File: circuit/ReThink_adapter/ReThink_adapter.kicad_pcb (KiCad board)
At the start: 2 copper layers, 69 parts, among them J1 FH34SRJ-34S-0.5SH(50), J2 FH34SRJ-6S-0.5SH(50), J3 Mezzanine, J4 XF3M(1)-3015-1B, J5 XF3M(1)-0815-1B, J6 FH34SRJ-40S-0.5SH(50), J7 FH52-40S-0.5SH, J8 XF3M(1)-1415-1B, U1 PCAL6416AHF, U2 LM2775DSG, U3 PCA9306, U4 TPS610333DRLR

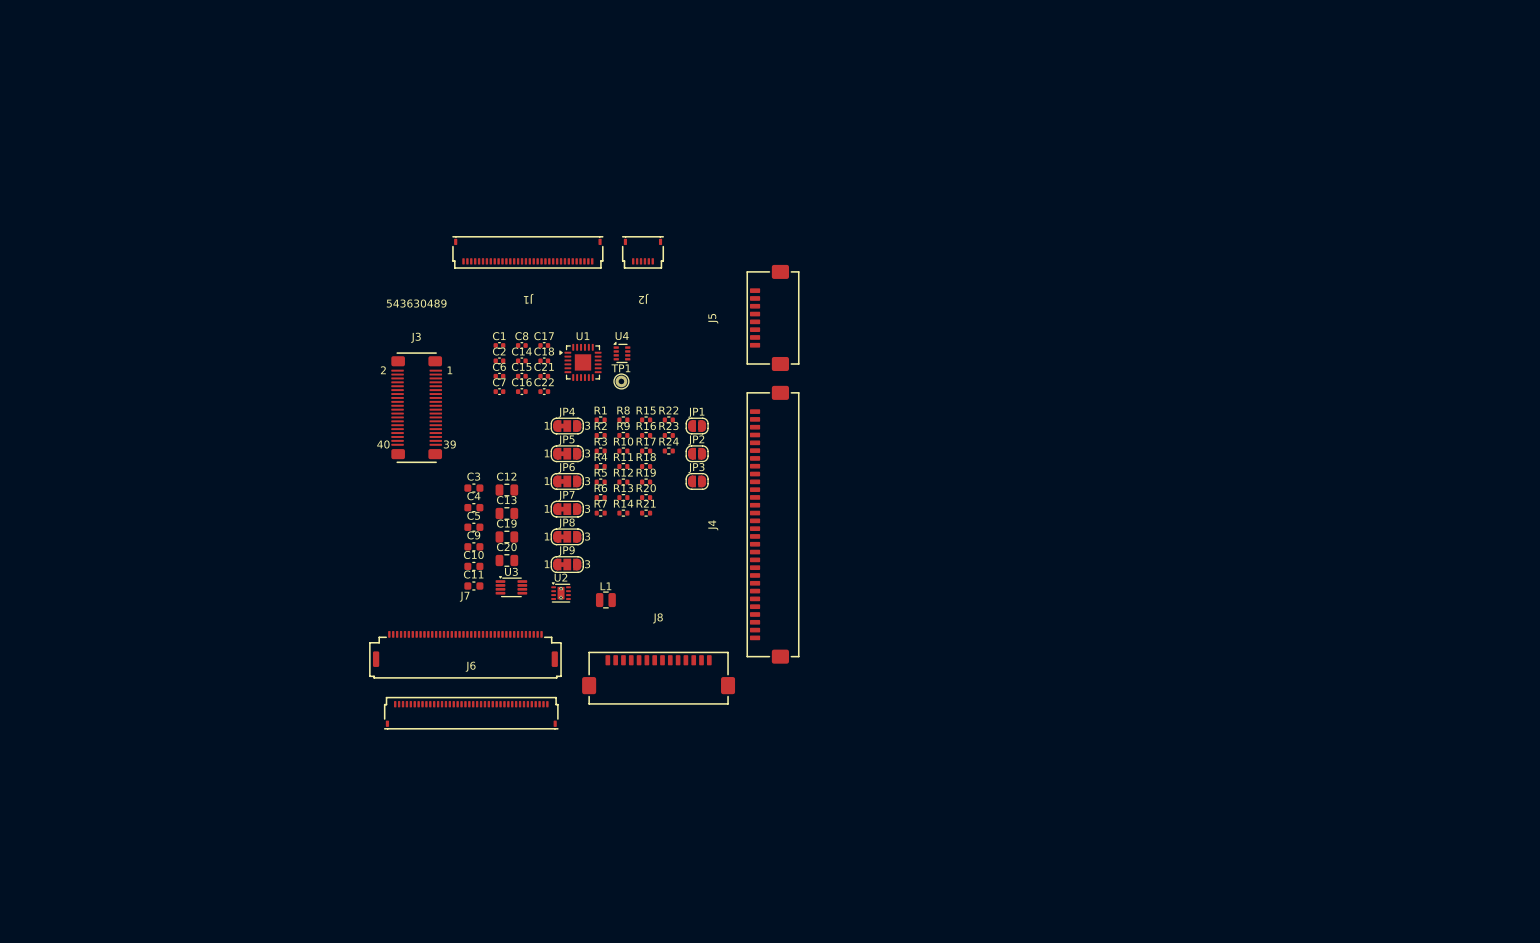
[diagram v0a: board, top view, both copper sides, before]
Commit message: group connectors on PCB
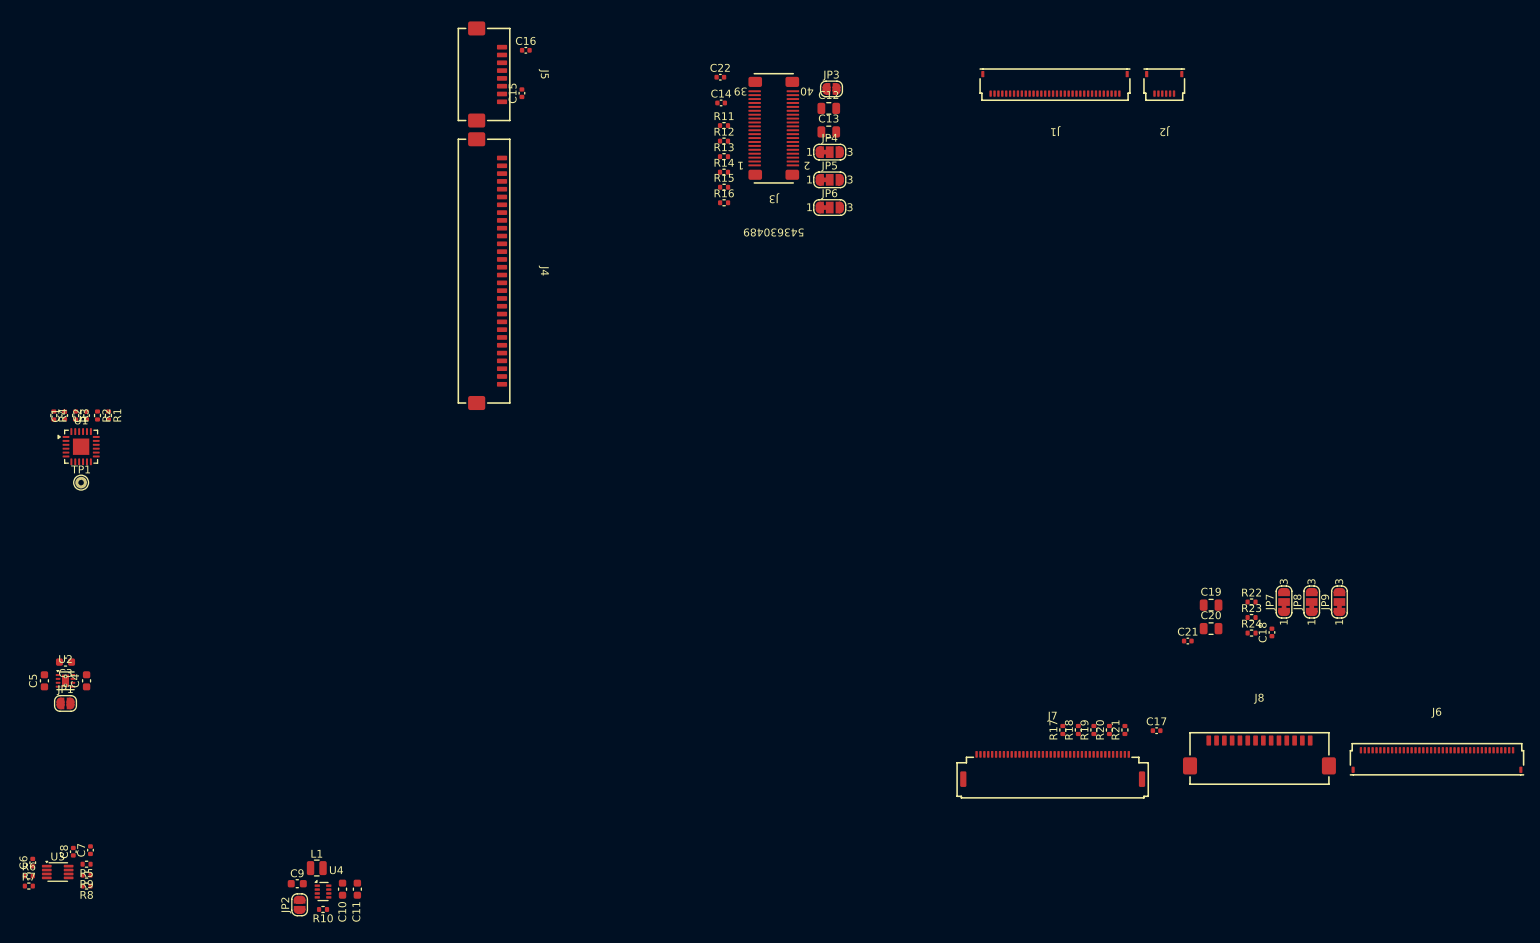
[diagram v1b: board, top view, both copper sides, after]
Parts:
- moved J6 123.9 mm to (212.8, 151.5)
- moved C18 99.5 mm to (191.6, 136.8), turned to 90 degrees
- moved JP9 99.1 mm to (200.2, 132.9), turned to 90 degrees
- moved JP8 95.8 mm to (196.7, 132.9), turned to 90 degrees
- moved C17 92.7 mm to (176.8, 149.4)
- moved JP7 92.6 mm to (193.2, 132.9), turned to 90 degrees
- moved R8 91.1 mm to (39.7, 169.3), turned to 180 degrees
- moved C19 90.7 mm to (183.8, 133.3)
- moved C20 90.7 mm to (183.8, 136.3)
- moved C21 89.2 mm to (180.8, 137.9)
- moved R9 88.9 mm to (39.7, 167.9), turned to 180 degrees
- moved JP1 88.4 mm to (37.0, 145.9)
- moved R6 87.9 mm to (32.3, 168.0)
- moved R7 87.5 mm to (32.3, 169.3)
- moved C8 86.7 mm to (38.0, 164.9), turned to 90 degrees
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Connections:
- J2 pad 1: GND -> VIN
- J2 pad 2: GND -> VIN
- J2 pad 5: VIN -> GND
- J2 pad 6: VIN -> GND
- J5 pad 1: TP1_PWR -> /TP1_DAT
- J5 pad 2: GND -> /TP1_RST
- J5 pad 3: /TP1_CLK -> /MIDDLE
- J5 pad 4: /LEFT -> /RIGHT
- J5 pad 5: /RIGHT -> /LEFT
- J5 pad 6: /MIDDLE -> /TP1_CLK
- J5 pad 7: /TP1_RST -> GND
- J5 pad 8: /TP1_DAT -> TP1_PWR
- J6 pad 10: /SENSE2 -> /HOTKEY
- J6 pad 11: /SENSE0 -> Net-(J6-Pin_11)
- J6 pad 12: /DRV4 -> Net-(J6-Pin_12)
- J6 pad 13: /DRV2 -> Net-(J6-Pin_13)
- J6 pad 14: /SENSE5 -> LED_3V3
- J6 pad 15: /DRV1 -> /DRV11
- J6 pad 16: /DRV3 -> /DRV8
- J6 pad 17: /DRV6 -> /DRV10
- J6 pad 18: /DRV7 -> /DRV12
- J6 pad 19: /DRV5 -> /DRV9
- J6 pad 20: /DRV15 -> /DRV13
- J6 pad 21: /DRV13 -> /DRV15
- J6 pad 22: /DRV9 -> /DRV5
- J6 pad 23: /DRV12 -> /DRV7
- J6 pad 24: /DRV10 -> /DRV6
- J6 pad 25: /DRV8 -> /DRV3
- J6 pad 26: /DRV11 -> /DRV1
- J6 pad 27: LED_3V3 -> /SENSE5
- J6 pad 28: Net-(J6-Pin_28) -> /DRV2
- J6 pad 29: Net-(J6-Pin_29) -> /DRV4
- J6 pad 3: /SENSE3 -> /DRV16
- J6 pad 30: Net-(J6-Pin_30) -> /SENSE0
- J6 pad 31: /HOTKEY -> /SENSE2
- J6 pad 32: GND -> /DRV0
- J6 pad 33: Net-(J6-Pin_33) -> /SENSE1
- J6 pad 34: GND -> /SENSE4
- J6 pad 35: /LEFT -> /DRV14
- J6 pad 36: /RIGHT -> /SENSE6
- J6 pad 37: /MIDDLE -> /SENSE7
- J6 pad 38: /DRV16 -> /SENSE3
- J6 pad 4: /SENSE7 -> /MIDDLE
- J6 pad 5: /SENSE6 -> /RIGHT
- J6 pad 6: /DRV14 -> /LEFT
- J6 pad 7: /SENSE4 -> GND
- J6 pad 8: /SENSE1 -> Net-(J6-Pin_8)
- J6 pad 9: /DRV0 -> GND
- J7 pad 26: Net-(J6-Pin_28) -> Net-(J6-Pin_13)
- J7 pad 27: Net-(J6-Pin_29) -> Net-(J6-Pin_12)
- J7 pad 28: Net-(J6-Pin_30) -> Net-(J6-Pin_11)
- J7 pad 31: Net-(J6-Pin_33) -> Net-(J6-Pin_8)
- J8 pad 1: TP2_PWR -> unconnected-(J8-Pin_1-Pad1)
- J8 pad 10: /PWM -> BL_5V
- J8 pad 11: /KBD_BL_DTCT -> /PWM
- J8 pad 12: GND -> /KBD_BL_DTCT
- J8 pad 13: (no net) -> GND
- J8 pad 14: (no net) -> unconnected-(J8-Pin_14-Pad14)
- J8 pad 2: /TP2_DAT -> TP2_PWR
- J8 pad 3: /TP2_RST -> /TP2_DAT
- J8 pad 4: /MIDDLE -> /TP2_RST
- J8 pad 5: /RIGHT -> /MIDDLE
- J8 pad 6: /LEFT -> /RIGHT
- J8 pad 7: GND -> /LEFT
- J8 pad 8: /TP2_CLK -> GND
- J8 pad 9: BL_5V -> /TP2_CLK
- R17 pad 1: Net-(J6-Pin_28) -> Net-(J6-Pin_13)
- R18 pad 1: Net-(J6-Pin_29) -> Net-(J6-Pin_12)
- R19 pad 1: Net-(J6-Pin_30) -> Net-(J6-Pin_11)
- R20 pad 1: Net-(J6-Pin_33) -> Net-(J6-Pin_8)
- R24 pad 2: GND -> unconnected-(R24-Pad2)
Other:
- board text added: "Connector orientation: Good Placement: Grouped"
- board text added: "Connector orientation: Good Placement: Not checked"
- board text added: "Connector orientation: Not checked Placement: Grouped"
- board text added: "Max height: 1.5mm"

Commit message: added JLCPCB rules
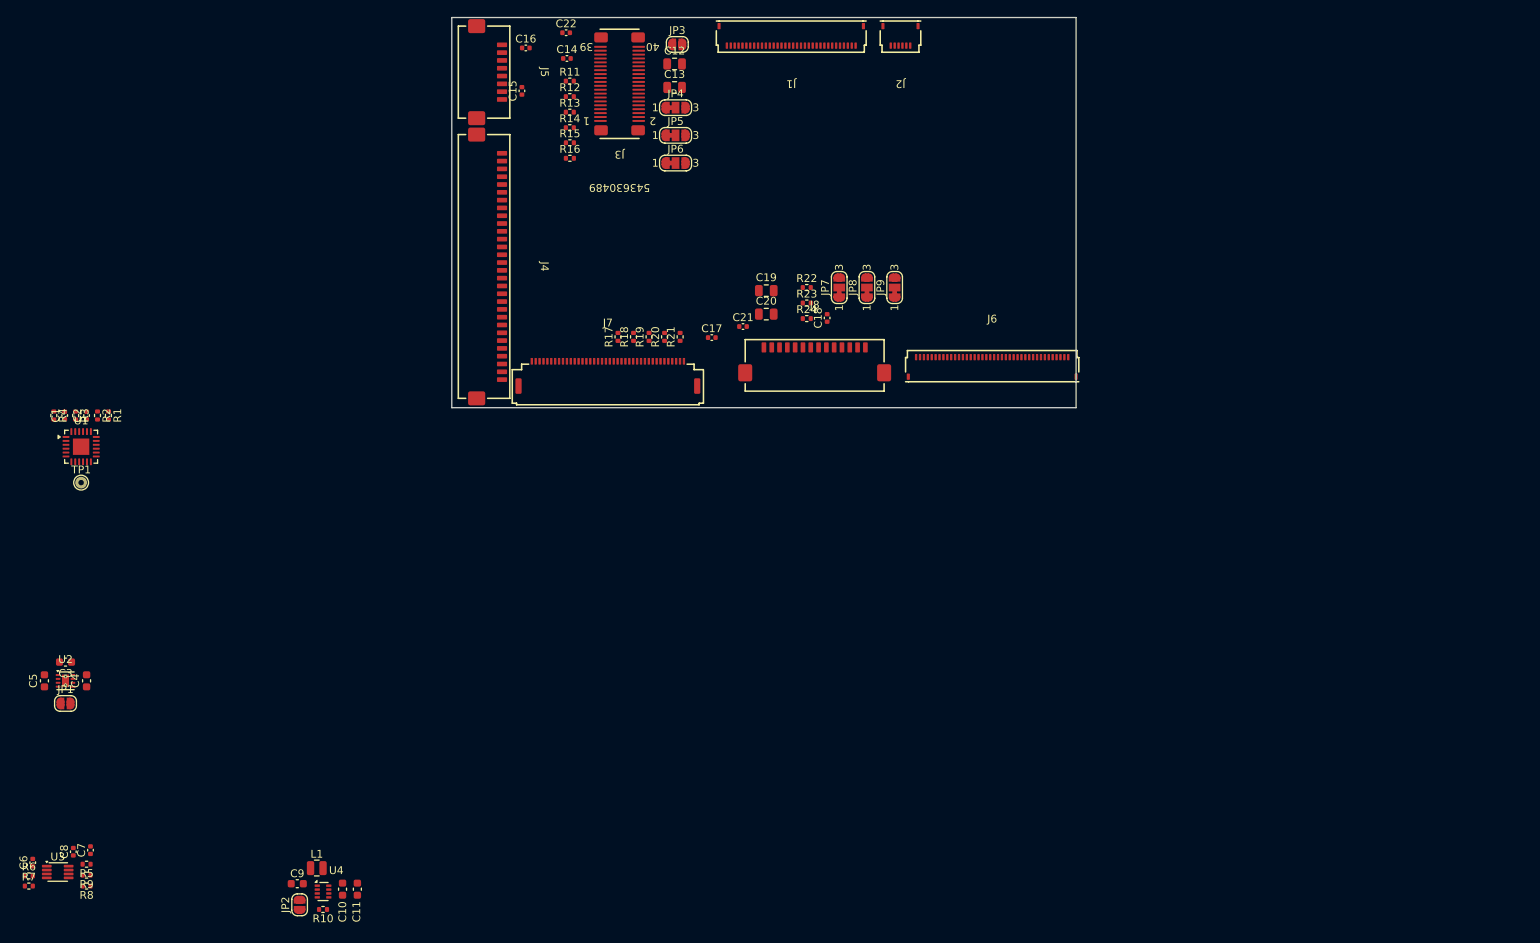
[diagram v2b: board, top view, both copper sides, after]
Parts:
- moved R17 76.1 mm to (107.8, 98.9)
- moved R19 76.1 mm to (111.8, 98.9)
- moved R20 76.1 mm to (113.8, 98.9)
- moved J6 76.1 mm to (155.8, 101.1)
- moved J7 76.1 mm to (106.5, 101.6)
- moved J8 76.1 mm to (133.0, 99.6)
- moved C17 76.1 mm to (119.8, 99.0)
- moved R18 76.1 mm to (109.8, 98.9)
- moved R21 76.1 mm to (115.8, 98.9)
- moved C19 69.8 mm to (126.8, 93.0)
- moved C20 69.8 mm to (126.8, 96.0)
- moved C18 69.8 mm to (134.6, 96.5)
- moved C21 69.8 mm to (123.8, 97.6)
- moved JP7 69.8 mm to (136.2, 92.6)
- moved JP8 69.8 mm to (139.7, 92.6)
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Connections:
- net Net-(U4-SW) renamed /SW
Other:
- board outline added: 80 x 50 mm

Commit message: lock connector placement on adapter PCB
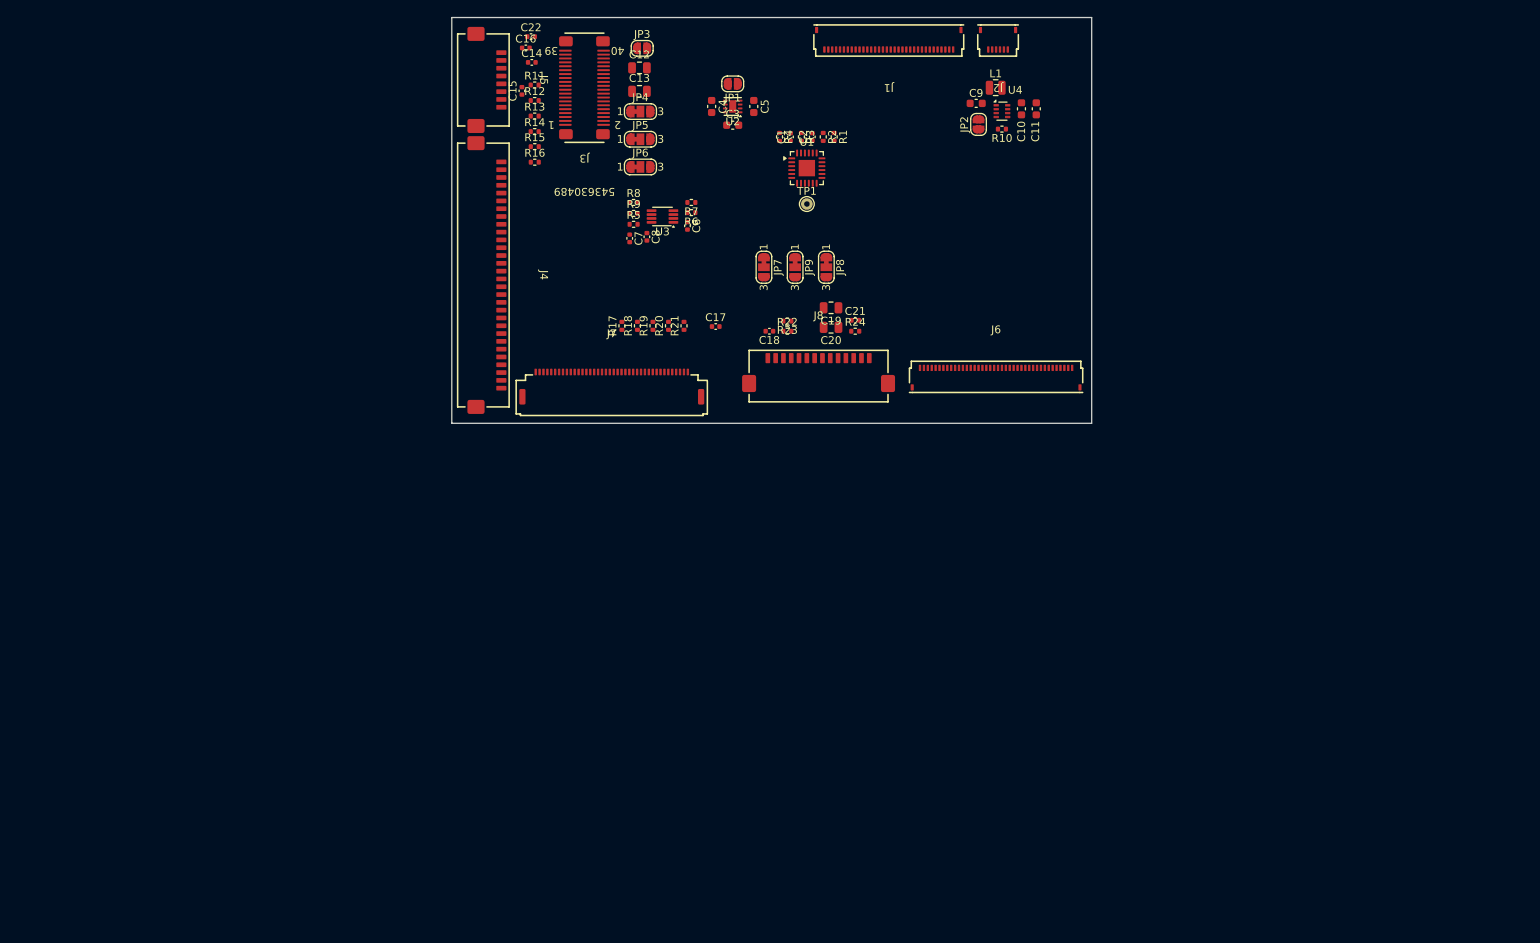
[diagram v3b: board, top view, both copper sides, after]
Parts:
- U2: footprint Package_SON:Texas_DSG0008A_WSON-8-1EP_2x2mm_P0.5mm_EP0.9x1.6mm_ThermalVias -> Package_SON:Texas_DSG0008A_WSON-8-1EP_2x2mm_P0.5mm_EP0.9x1.6mm
- moved C10 132.5 mm to (159.5, 69.7)
- moved C11 132.5 mm to (161.4, 69.7)
- moved C9 132.5 mm to (153.7, 69.0)
- moved JP2 132.5 mm to (154.0, 71.7)
- moved L1 132.5 mm to (156.2, 67.0)
- moved R10 132.5 mm to (157.0, 72.3)
- moved U4 132.5 mm to (157.0, 70.0)
- moved R7 122.0 mm to (117.2, 81.7), turned to 180 degrees
- moved R6 120.1 mm to (117.2, 83.0), turned to 180 degrees
- moved C6 117.0 mm to (116.7, 84.7), turned to -90 degrees
- moved C5 117.0 mm to (125.2, 69.4), turned to -90 degrees
- moved JP1 116.7 mm to (122.5, 66.5), turned to 180 degrees
- moved U3 114.3 mm to (113.5, 83.5), turned to 180 degrees
- moved U2 112.8 mm to (122.5, 69.4), turned to 180 degrees
- moved R8 112.2 mm to (109.8, 81.7), turned to 0 degrees
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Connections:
- R24 pad 2: unconnected-(R24-Pad2) -> GND
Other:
- board size 80 x 50 mm -> 82 x 52 mm
- board text added: "Connector orientation: Good Placement: Locked"
- board text added: "Connector orientation: Not checked Placement: Locked"
- board text removed: "Connector orientation: Good Placement: Grouped"
- board text removed: "Connector orientation: Good Placement: Not checked"
- board text removed: "Connector orientation: Not checked Placement: Grouped"

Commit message: start routing
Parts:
- added C23: 0.1u, Capacitor_SMD:C_0402_1005Metric, F.Cu at (159.5, 99.6)
- moved R17 31.9 mm to (136.5, 82.6), turned to 180 degrees
- moved R18 30.9 mm to (136.5, 81.2), turned to 180 degrees
- moved R19 30.0 mm to (136.5, 79.8), turned to 180 degrees
- moved R20 29.3 mm to (136.5, 78.4), turned to 180 degrees
- moved R21 28.8 mm to (136.5, 77.0), turned to 180 degrees
- moved C7 18.6 mm to (115.7, 68.8), turned to 180 degrees
- moved R5 17.0 mm to (117.5, 69.3), turned to -90 degrees
- moved R9 16.5 mm to (118.9, 69.3), turned to -90 degrees
- moved JP5 16.4 mm to (121.5, 61.3), turned to -90 degrees
- moved R8 16.2 mm to (120.3, 69.3), turned to -90 degrees
- moved R16 16.2 mm to (109.4, 66.0), turned to 180 degrees
- moved JP6 16.1 mm to (113.5, 61.3), turned to -90 degrees
- moved C8 15.7 mm to (115.9, 71.0), turned to 180 degrees
- moved R14 15.5 mm to (109.4, 63.2), turned to 180 degrees
- moved C13 14.5 mm to (96.8, 62.8), turned to 180 degrees
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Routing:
- net Net-(JP3-B): track 0.00 -> 24.0 mm
- net TP_3V3: track 0.00 -> 20.7 mm
- net TP2_PWR: track 0.00 -> 14.2 mm
- net VIN: track 0.00 -> 12.8 mm
- net TP1_PWR: track 0.00 -> 12.8 mm
- net BL_5V: track 0.00 -> 10.3 mm
- net /TP1_RST: track 0.00 -> 8.98 mm
- net Net-(J3-Pad21): track 0.00 -> 6.49 mm
- net TP_5V: track 0.00 -> 6.09 mm
- net Net-(J3-Pad23): track 0.00 -> 5.77 mm
- net LED_3V3: track 0.00 -> 5.67 mm
- net GND: track 0.00 -> 5.23 mm
- net /PWM: track 0.00 -> 5.15 mm
- net Net-(C22-Pad1): track 0.00 -> 5.02 mm
- net /TP2_RST: track 0.00 -> 4.75 mm
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
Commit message: routing mostly done
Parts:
- added H1: M2.5, MountingHole:MountingHole_2.7mm_M2.5_DIN965_Pad, F.Cu at (165.5, 61.0)
- added H2: M2.5, MountingHole:MountingHole_2.7mm_M2.5_DIN965_Pad, F.Cu at (165.5, 96.0)
- added H3: M2.5, MountingHole:MountingHole_2.7mm_M2.5_DIN965_Pad, F.Cu at (108.5, 96.0)
- added H4: M2.5, MountingHole:MountingHole_2.7mm_M2.5_DIN965_Pad, F.Cu at (96.5, 80.0)
- added H5: M2, MountingHole:MountingHole_2.2mm_M2_ISO14580, F.Cu at (123.5, 98.0)
- added H6: M2, MountingHole:MountingHole_2.2mm_M2_ISO14580, F.Cu at (143.5, 98.0)
- moved C11 7.32 mm to (156.8, 75.4), turned to 180 degrees
- moved C10 4.66 mm to (156.8, 73.5), turned to 180 degrees
- moved L1 4.60 mm to (159.5, 70.2), turned to -90 degrees
- moved C4 4.58 mm to (128.5, 70.7), turned to 0 degrees
- moved C3 4.16 mm to (130.9, 68.0), turned to 90 degrees
- moved C9 4.02 mm to (157.5, 67.7), turned to 90 degrees
- moved JP2 3.79 mm to (154.8, 68.0), turned to 180 degrees
- moved JP1 3.47 mm to (125.6, 68.0), turned to -90 degrees
- moved C5 3.19 mm to (128.5, 65.3), turned to 0 degrees
- moved R10 3.09 mm to (154.2, 71.0), turned to 90 degrees
- moved U4 1.12 mm to (156.5, 71.0), turned to -90 degrees
- moved U2 1.00 mm to (128.5, 68.0), turned to -90 degrees
- moved C17 0.90 mm to (110.0, 100.6), turned to 0 degrees
- turned C16 to 90 degrees
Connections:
- J4 pad 3: /RIGHT -> /TP1_RIGHT
- J4 pad 4: /MIDDLE -> /TP1_MIDDLE
- J4 pad 5: /LEFT -> /TP1_LEFT
- J5 pad 3: /MIDDLE -> /TP1_MIDDLE
- J5 pad 4: /RIGHT -> /TP1_RIGHT
- J5 pad 5: /LEFT -> /TP1_LEFT
- J6 pad 4: /MIDDLE -> /TP2_MIDDLE
- J6 pad 5: /RIGHT -> /TP2_RIGHT
- J6 pad 6: /LEFT -> /TP2_LEFT
- J7 pad 33: /LEFT -> /TP2_LEFT
- J7 pad 34: /RIGHT -> /TP2_RIGHT
- J7 pad 35: /MIDDLE -> /TP2_MIDDLE
- J8 pad 5: /MIDDLE -> /TP2_MIDDLE
- J8 pad 6: /RIGHT -> /TP2_RIGHT
- J8 pad 7: /LEFT -> /TP2_LEFT
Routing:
- net GND: track 5.23 -> 239.0 mm, vias 0 -> 323
- net /SENSE0: track 0.00 -> 151.7 mm, vias 0 -> 4
- net /SENSE6: track 0.00 -> 150.1 mm, vias 0 -> 6
- net /SENSE7: track 0.00 -> 149.7 mm, vias 0 -> 6
- net /DRV13: track 0.00 -> 149.6 mm, vias 0 -> 5
- net /SENSE2: track 0.00 -> 149.2 mm, vias 0 -> 6
- net /SENSE4: track 0.00 -> 149.2 mm, vias 0 -> 6
- net /SENSE1: track 0.00 -> 149.1 mm, vias 0 -> 4
- net /DRV11: track 0.00 -> 148.3 mm, vias 0 -> 5
- net /SENSE5: track 0.00 -> 147.9 mm, vias 0 -> 5
- net /DRV12: track 0.00 -> 147.5 mm, vias 0 -> 5
- net /DRV8: track 0.00 -> 146.4 mm, vias 0 -> 5
- net /DRV9: track 0.00 -> 145.9 mm, vias 0 -> 5
- net /SENSE3: track 0.00 -> 145.8 mm, vias 0 -> 6
- net /DRV14: track 0.00 -> 145.6 mm, vias 0 -> 5
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- added copper zone on B.Cu, net GND
- added copper zone on F.Cu, net GND
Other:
- outline, holes or cut-outs redrawn
- board text added: "M2"
- board text added: "M2.5"
